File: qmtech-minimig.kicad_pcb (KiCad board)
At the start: 4 copper layers, 142.2 x 91.9 mm, 148 parts, among them IC1 ESP32-WROVER-B_(16MB), J1 DB9_Male, J2 DB9_Male, J3 SCHA5B0200, J4 10118193-0001LF, J5 AUDIO-CONNECTOR-6P-SMD-344003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, J6 Mini-DIN-6, J7 Conn_02x13_Odd_Even, J8 Conn_01x04, J9 47151-0001, Q1 MMBT2222A, Q2 MMBT2222A, Q3 BSS84, SW1 SW_Push, U2 QM_XC7A35T_DDR3, U3 LT1963AxST-1.8, U4 INTERFACE-CP2102-GMR(QFN28), U5 MT3608, U6 TXS0108EPWR, U7 TXS0108EPWR

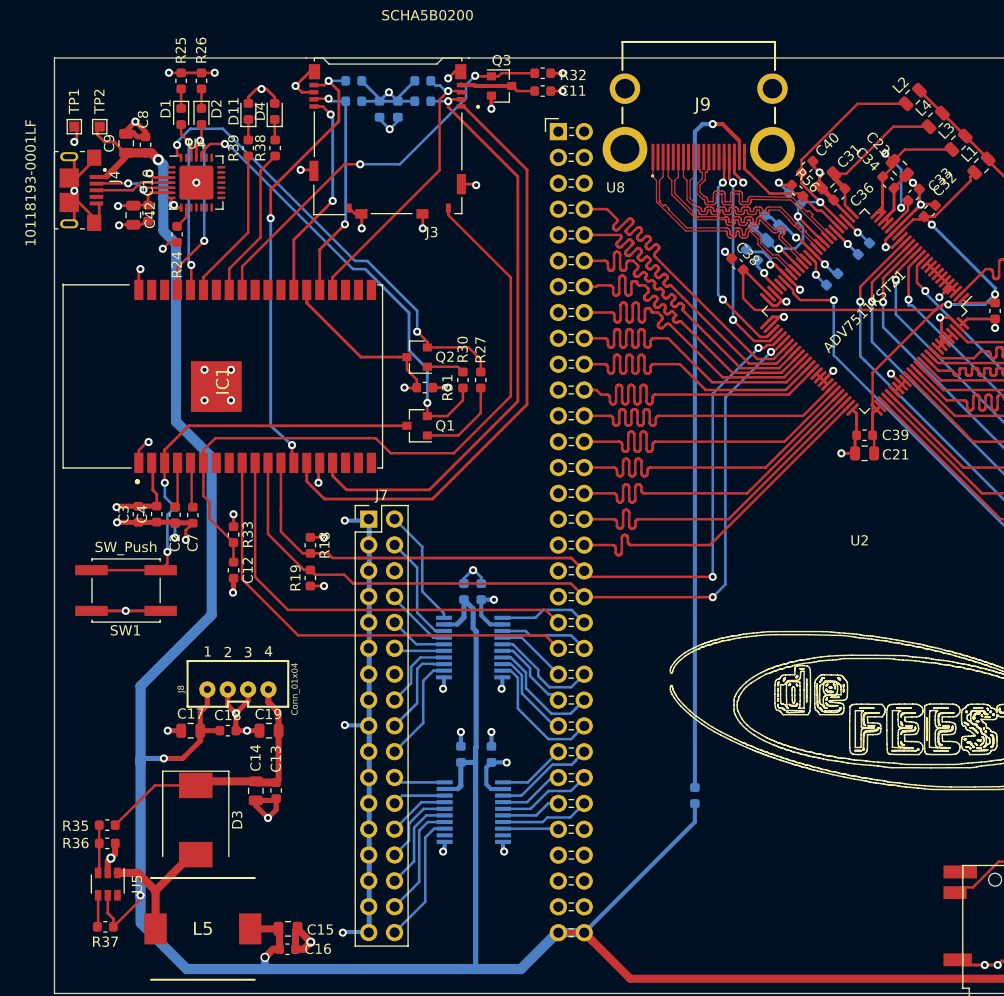
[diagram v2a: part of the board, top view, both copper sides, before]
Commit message: Moved the micro USB connector to the bottom of the board, so the D+ and D- do not have to cross to the IC.
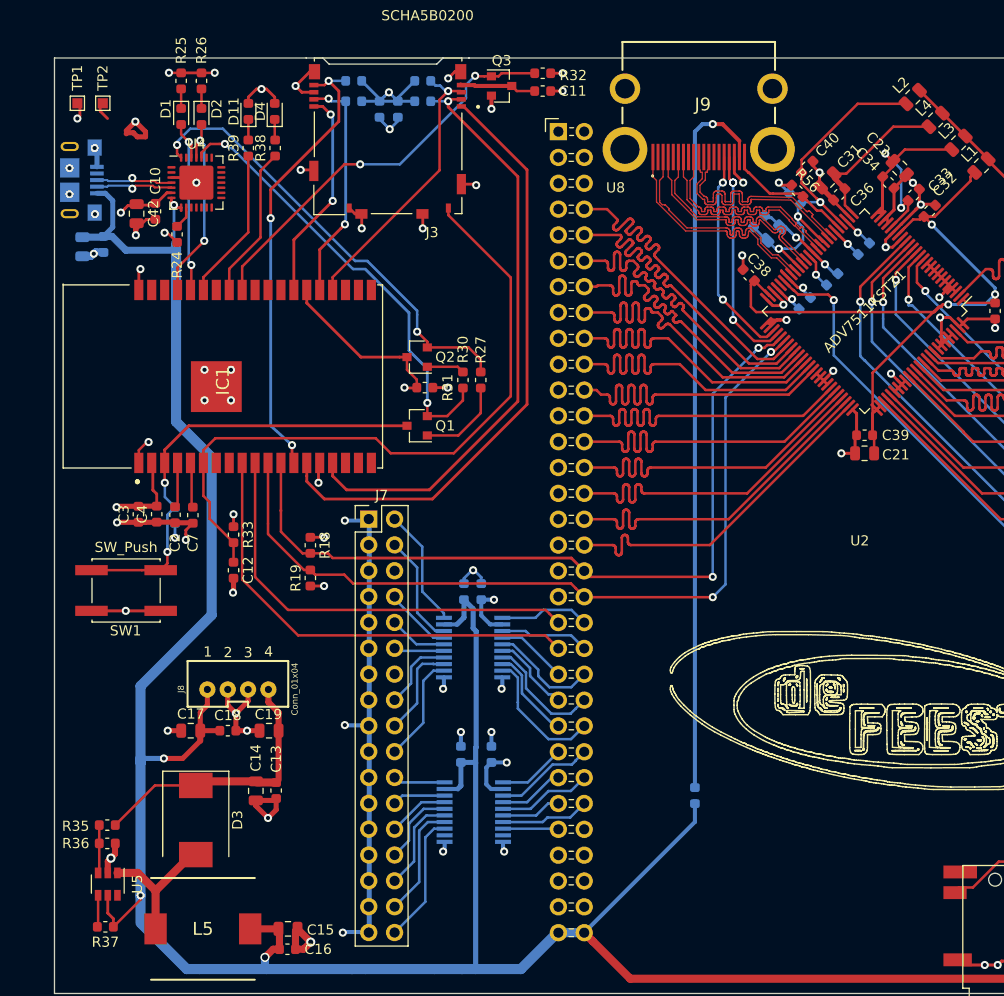
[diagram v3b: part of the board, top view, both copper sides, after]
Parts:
- C8, C9, J4: moved to B.Cu
- moved C9 11.0 mm to (53.5, 81.8), turned to 270 degrees
- moved C8 10.6 mm to (55.6, 81.6), turned to 270 degrees
- moved C1 7.04 mm to (124.5, 87.4), turned to 225 degrees
- moved TP1 2.32 mm to (53.0, 67.7)
- moved TP2 2.32 mm to (55.5, 67.7)
- moved C38 1.55 mm to (119.0, 84.6)
- moved J4 1.00 mm to (52.3, 75.2), turned to 90 degrees
- moved C10 0.75 mm to (60.7, 78.3)
- moved C42 0.36 mm to (58.9, 78.5)
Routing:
- net GND: track 331.3 -> 317.1 mm, vias 84 -> 86
- net VIN5V: track 327.2 -> 323.8 mm, vias 5 -> 4
- net ADV_DVDD: track 78.7 -> 76.1 mm
- net 3V3: track 124.2 -> 123.2 mm
- net /MCU/D+: track 7.22 -> 7.70 mm, vias 0 -> 1
- net /MCU/D-: track 7.23 -> 7.70 mm, vias 2 -> 1

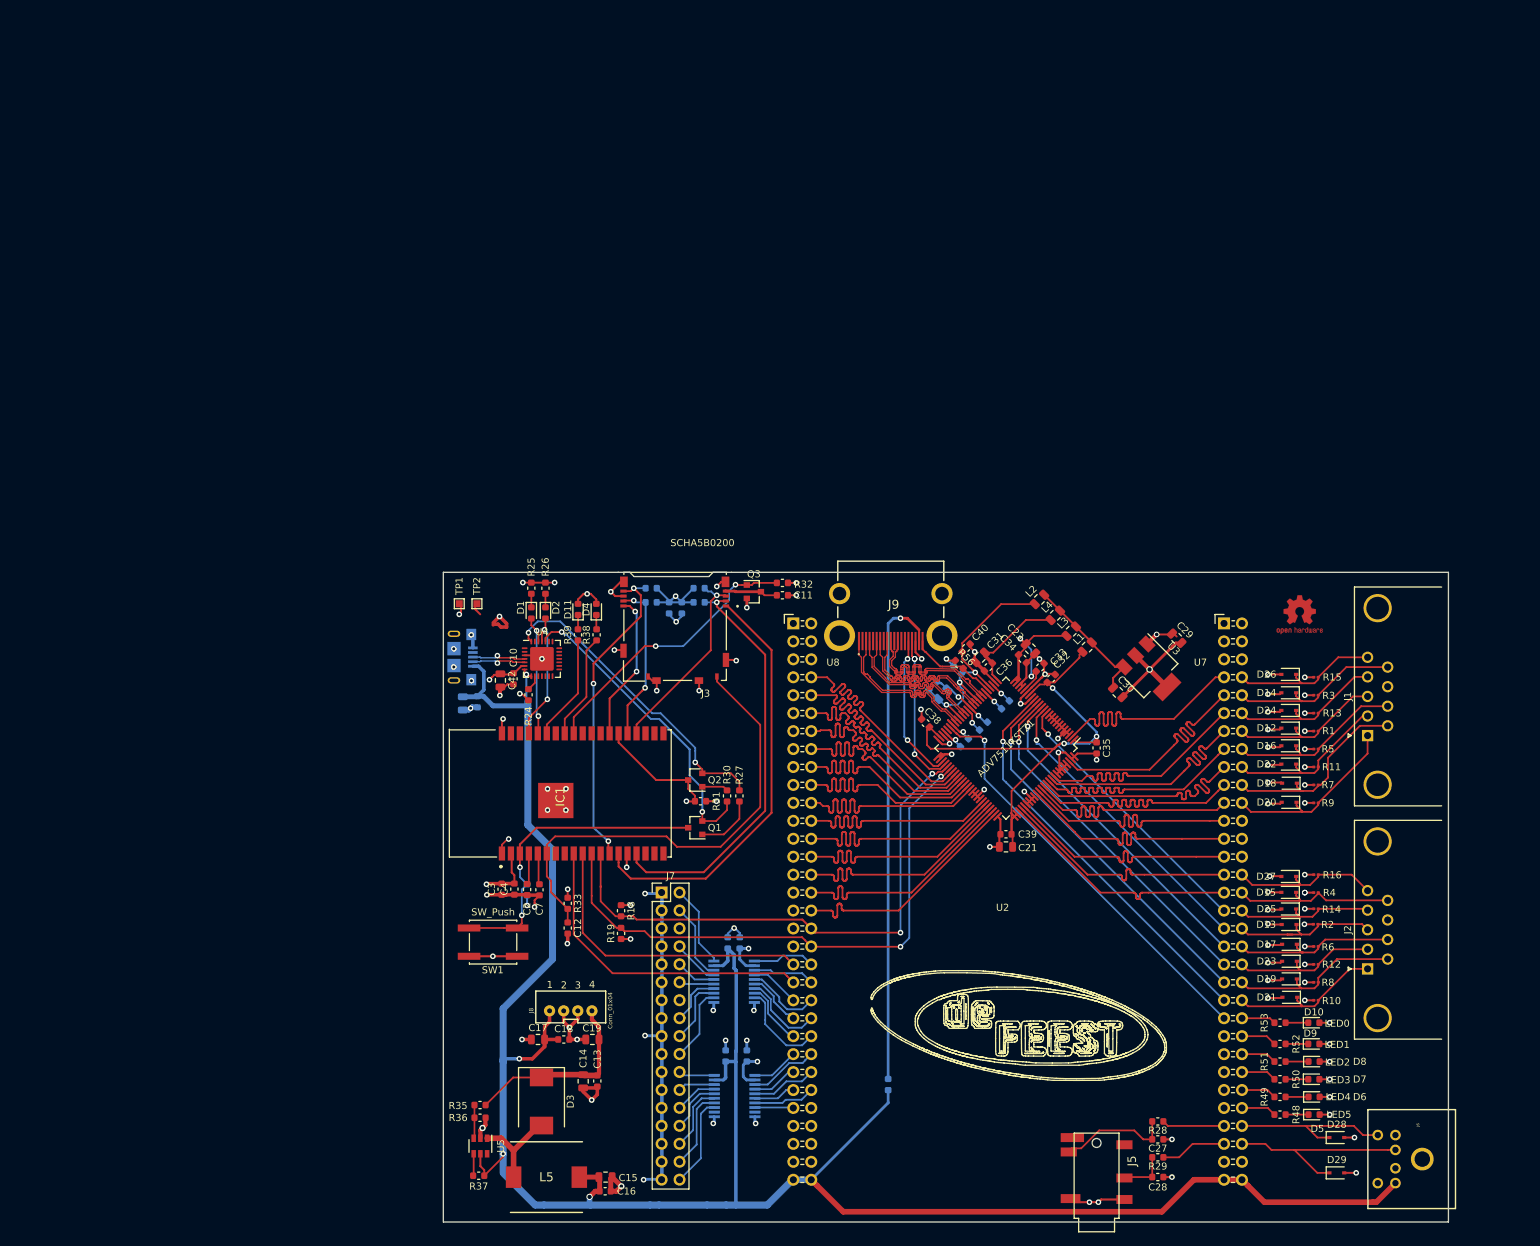
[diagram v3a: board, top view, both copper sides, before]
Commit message: Add the External floppy interface. Routed the HDMI tracks + match impendence.
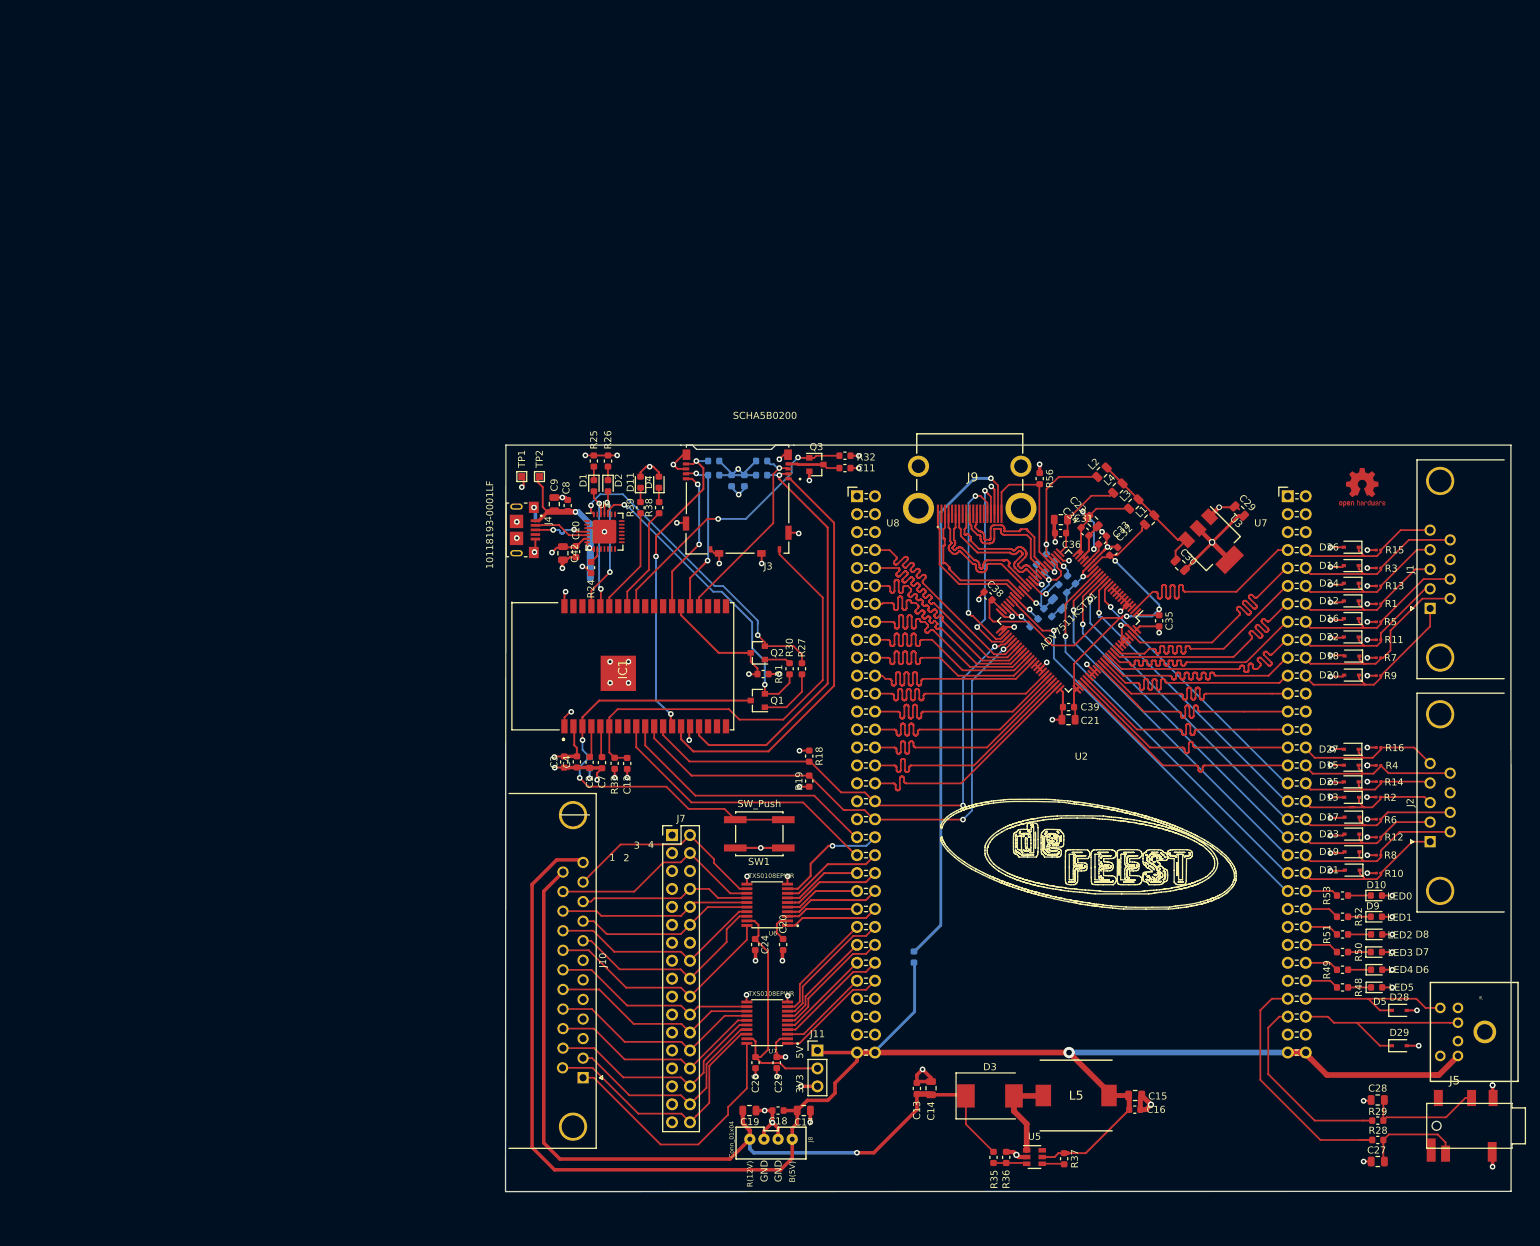
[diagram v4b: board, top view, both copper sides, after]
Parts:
- added J10: DB23_Female_MountingHoles, c64-wing-kicad:DSUB-23_Female_Horizontal_P2.77x2.84mm_EdgePinOffset7.70mm_Housed_MountingHolesOffset9.12mm, F.Cu at (70.6, 134.8)
- added J11: Conn_01x03_Male, Connector_PinHeader_2.54mm:PinHeader_1x03_P2.54mm_Vertical, F.Cu at (103.7, 130.9)
- C20, C24, C25, C26, C8, C9, J4, U6, U7: moved to F.Cu
- C27, C28: footprint Capacitor_SMD:C_0603_1608Metric -> Capacitor_SMD:C_0805_2012Metric
- C40: moved to B.Cu
- moved R37 82.9 mm to (138.7, 146.2), turned to 270 degrees
- moved U5 78.4 mm to (134.5, 146.0), turned to 0 degrees
- moved L5 75.9 mm to (140.4, 137.3)
- moved C15 75.8 mm to (148.7, 137.3)
- moved C16 75.8 mm to (148.7, 139.3)
- moved R36 74.7 mm to (130.5, 146.1), turned to 90 degrees
- moved R35 73.0 mm to (128.7, 146.1), turned to 270 degrees
- moved D3 63.5 mm to (128.2, 137.4), turned to 0 degrees
- moved J5 54.3 mm to (197.0, 141.6), turned to 0 degrees
- moved C14 49.2 mm to (119.8, 136.3), turned to 90 degrees
- moved C13 45.2 mm to (117.8, 136.3), turned to 90 degrees
- moved SW1 40.7 mm to (95.5, 100.3)
- moved C17 38.9 mm to (101.8, 139.4), turned to 180 degrees
- moved R18 34.5 mm to (102.6, 89.3)
- moved J8 34.3 mm to (97.2, 144.0), turned to 180 degrees
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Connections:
- C24 pad 2: VIN5V -> /Floppy/VIOSEL
- C26 pad 2: VIN5V -> /Floppy/VIOSEL
- C8 pad 1: VIN5V -> VUSB5V
- C9 pad 1: VIN5V -> VUSB5V
- IC1 pad 29: Net-(IC1-Pad29) -> ADV_INT
- J4 pad 1: VIN5V -> VUSB5V
- TP2 pad 1: VIN5V -> VUSB5V
- U2 pad U756: Net-(U2-PadU756) -> EXP_35
- U4 pad 7: VIN5V -> VUSB5V
- U4 pad 8: VIN5V -> VUSB5V
- U6 pad 1: EXP_02 -> EXP_20
- U6 pad 12: H_EXP_20 -> H_EXP_02
- U6 pad 13: H_EXP_18 -> H_EXP_04
- U6 pad 14: H_EXP_16 -> H_EXP_08
- U6 pad 15: H_EXP_12 -> H_EXP_10
- U6 pad 16: H_EXP_10 -> H_EXP_12
- U6 pad 17: H_EXP_08 -> H_EXP_16
- U6 pad 18: H_EXP_04 -> H_EXP_18
- U6 pad 19: VIN5V -> /Floppy/VIOSEL
- U6 pad 20: H_EXP_02 -> H_EXP_20
- U6 pad 3: EXP_04 -> EXP_18
- U6 pad 4: EXP_08 -> EXP_16
- U6 pad 5: EXP_10 -> EXP_12
- U6 pad 6: EXP_12 -> EXP_10
- U6 pad 7: EXP_16 -> EXP_08
- U6 pad 8: EXP_18 -> EXP_04
- U6 pad 9: EXP_20 -> EXP_02
- U7 pad 1: EXP_22 -> EXP_35
- U7 pad 12: Net-(U7-Pad12) -> H_EXP_22
- U7 pad 13: H_EXP_34 -> H_EXP_24
- U7 pad 14: H_EXP_32 -> H_EXP_26
- U7 pad 15: H_EXP_30 -> H_EXP_28
- U7 pad 16: H_EXP_28 -> H_EXP_30
- U7 pad 17: H_EXP_26 -> H_EXP_32
- U7 pad 18: H_EXP_24 -> H_EXP_34
- U7 pad 19: VIN5V -> /Floppy/VIOSEL
- U7 pad 20: H_EXP_22 -> H_EXP_35
- U7 pad 3: EXP_24 -> EXP_34
- U7 pad 4: EXP_26 -> EXP_32
- U7 pad 5: EXP_28 -> EXP_30
- U7 pad 6: EXP_30 -> EXP_28
- U7 pad 7: EXP_32 -> EXP_26
- U7 pad 8: EXP_34 -> EXP_24
- U7 pad 9: Net-(U7-Pad9) -> EXP_22
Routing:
- net VIN12V: track 27.4 -> 123.3 mm, vias 0 -> 1
- net VIN5V: track 323.8 -> 244.5 mm, vias 4 -> 1
- net GND: track 317.1 -> 262.6 mm, vias 86 -> 84
- net H_EXP_35: track 0.00 -> 37.4 mm
- net /Floppy/VIOSEL: track 0.00 -> 35.7 mm
- net AUDIO_LEFT: track 8.85 -> 33.8 mm
- net H_EXP_24: track 5.23 -> 29.8 mm
- net H_EXP_26: track 6.05 -> 30.5 mm
- net H_EXP_34: track 13.3 -> 37.5 mm
- net VUSB5V: track 0.00 -> 24.2 mm, vias 0 -> 2
- net H_EXP_22: track 5.12 -> 29.1 mm
- net H_EXP_20: track 10.6 -> 34.1 mm
- net H_EXP_28: track 7.78 -> 31.2 mm
- net H_EXP_30: track 9.52 -> 32.8 mm
- net H_EXP_16: track 8.27 -> 30.7 mm
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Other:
- board size 142.2 x 91.9 mm -> 142.3 x 105.7 mm
- net class HDMI: clearance 0.1 -> 0.15; trace_width 0.1 -> 0.28; via_dia 0.8 -> 0.4; via_drill 0.4 -> 0.3
